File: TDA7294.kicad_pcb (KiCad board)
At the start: 2 copper layers, 81 x 58 mm, 38 parts, among them J1 PAWER, J2 OUT, J3 IN, U1 TDA7294, U2 TDA7294

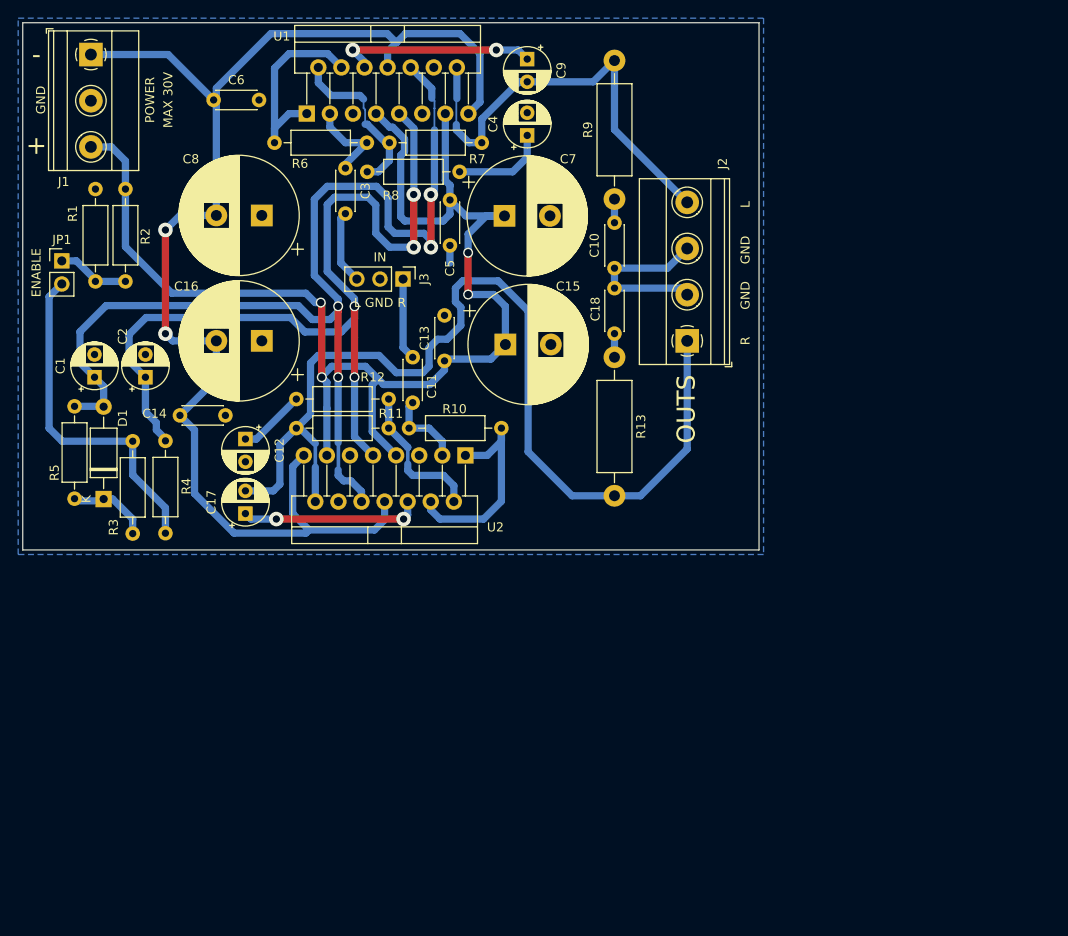
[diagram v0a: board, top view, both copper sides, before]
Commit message: agregando huecos para montaje
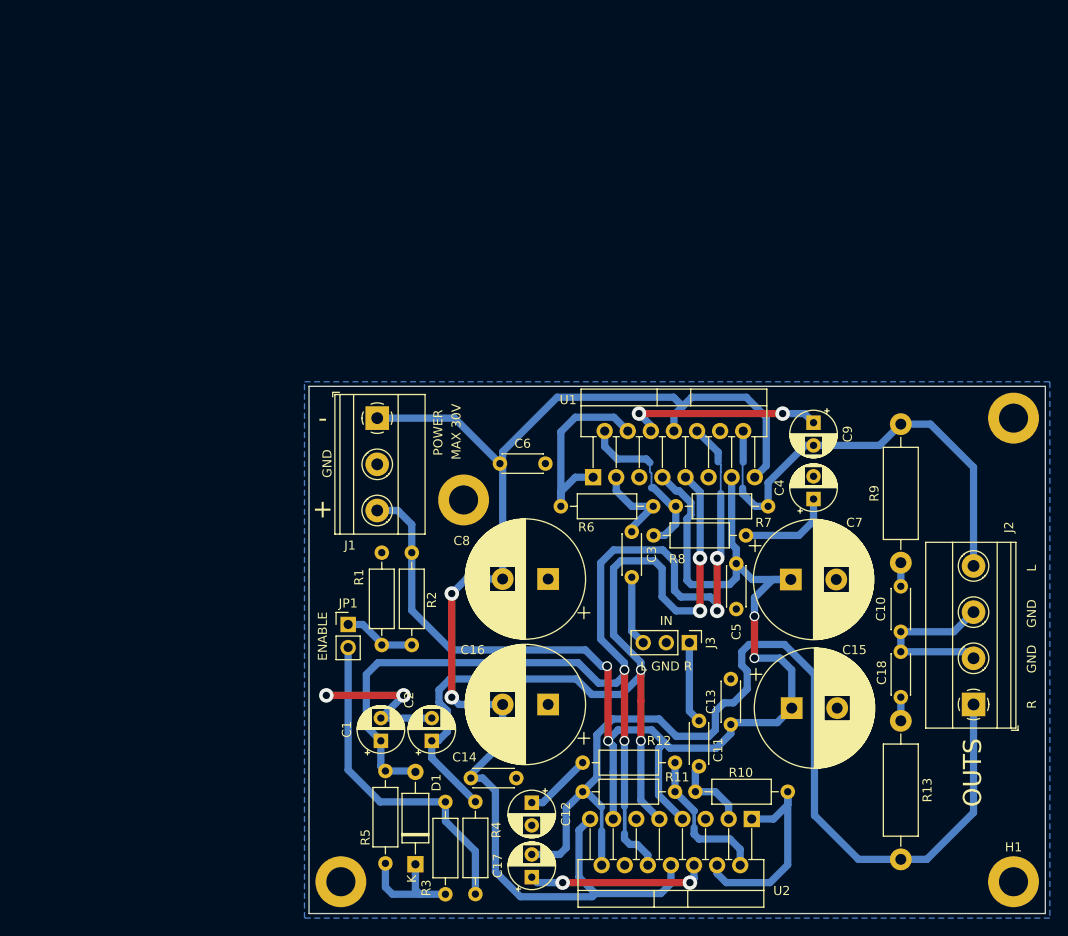
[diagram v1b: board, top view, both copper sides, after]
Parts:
- added H1: MH, MountingHole:MountingHole_3.2mm_M3_DIN965_Pad, F.Cu at (184.5, 124.5)
- added H2: MH, MountingHole:MountingHole_3.2mm_M3_DIN965_Pad, F.Cu at (110.5, 124.5)
- added H3: MH, MountingHole:MountingHole_3.2mm_M3_DIN965_Pad, F.Cu at (184.5, 73.5)
- added H4: MH, MountingHole:MountingHole_3.2mm_M3_DIN965_Pad, F.Cu at (124.0, 82.5)
- moved D1 52.8 mm to (118.7, 122.6)
- moved R5 52.7 mm to (115.4, 112.3)
- moved R3 52.5 mm to (122.0, 125.9)
- moved R4 52.3 mm to (125.3, 115.7)
- moved C14 51.1 mm to (124.8, 113.1)
- moved C16 50.9 mm to (133.3, 105.0)
- moved C4 50.9 mm to (162.5, 82.4)
- moved C8 50.9 mm to (133.3, 91.2)
- moved R7 50.9 mm to (144.9, 86.4)
- moved R9 50.9 mm to (172.1, 89.4)
- moved C1 50.9 mm to (114.9, 109.0)
- moved C10 50.9 mm to (172.1, 97.0)
- moved C11 50.9 mm to (149.9, 111.8)
- moved C12 50.9 mm to (131.5, 115.8)
- moved C13 50.9 mm to (153.4, 107.2)
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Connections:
- U1 pad 11: (no net) -> unconnected-(U1-Pad11)
- U1 pad 12: (no net) -> unconnected-(U1-Pad12)
- U1 pad 5: (no net) -> unconnected-(U1-Pad5)
- U2 pad 11: (no net) -> unconnected-(U2-Pad11)
- U2 pad 12: (no net) -> unconnected-(U2-Pad12)
- U2 pad 5: (no net) -> unconnected-(U2-Pad5)
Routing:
- net GND: track 68.0 -> 83.7 mm, vias 0 -> 2
- net Net-(D1-Pad1): track 9.49 -> 13.1 mm
- net /MUTE: track 119.0 -> 121.0 mm
- net /OUT1: track 49.1 -> 51.0 mm
- net /STBY: track 100.6 -> 99.7 mm
- net Net-(JP1-Pad2): track 37.8 -> 37.1 mm
- net /OUT2: track 112.1 -> 111.6 mm
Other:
- board text added: "0"
- board text added: "0 mm"
- board text added: "0.01 mm"
- board text added: "0.02"
- board text added: "0.035 mm"
- board text added: "0.2000 mm / 0.0000 mm"
- board text added: "0.3000 mm"
- board text added: "1"
- board text added: "1.51 mm"
- board text added: "1.6000 mm"
- board text added: "2"
- board text added: "3.3"
- board text added: "4.5"
- board text added: "81.0000 mm x 58.0000 mm"
- board text added: "B.Cu"
- board text added: "B.Mask"
- board text added: "B.Paste"
- board text added: "B.Silkscreen"
- board text added: "BOARD CHARACTERISTICS"
- board text added: "Black"
- board text added: "Board Thickness:"
- board text added: "Board overall dimensions:"
- board text added: "Bottom Silk Screen"
- board text added: "Bottom Solder Mask"
- board text added: "Bottom Solder Paste"
- board text added: "Castellated pads:"
- board text added: "Color"
- board text added: "Copper Finish:"
- board text added: "Copper Layer Count:"
- board text added: "Dielectric 1"
- board text added: "Direct Printing"
- board text added: "Edge card connectors:"
- board text added: "Epsilon R"
- board text added: "F.Cu"
- board text added: "F.Mask"
- board text added: "F.Paste"
- board text added: "F.Silkscreen"
- board text added: "FR4"
- board text added: "HAL SnPb"
- board text added: "Impedance Control:"
- board text added: "Layer Name"
- board text added: "Liquid Ink"
- board text added: "Loss Tangent"
- board text added: "Material"
- board text added: "Min hole diameter:"
- board text added: "Min track/spacing:"
- board text added: "No"
- board text added: "Plated Board Edge:"
- board text added: "Thickness (mm)"
- board text added: "Top Silk Screen"
- board text added: "Top Solder Mask"
- board text added: "Top Solder Paste"
- board text added: "Type"
- board text added: "White"
- board text added: "copper"
- board text added: "core"

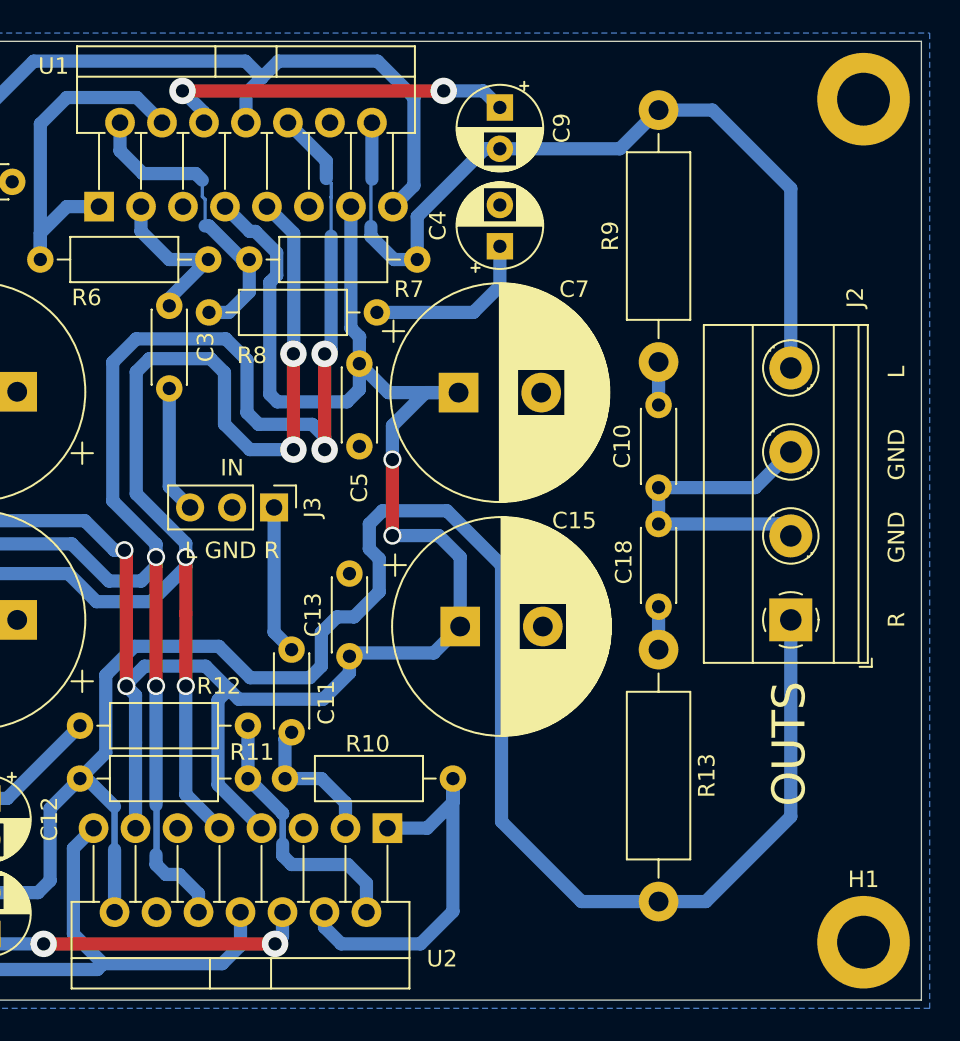
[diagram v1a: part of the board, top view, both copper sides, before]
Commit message: add version puenteable y archivos en pdf
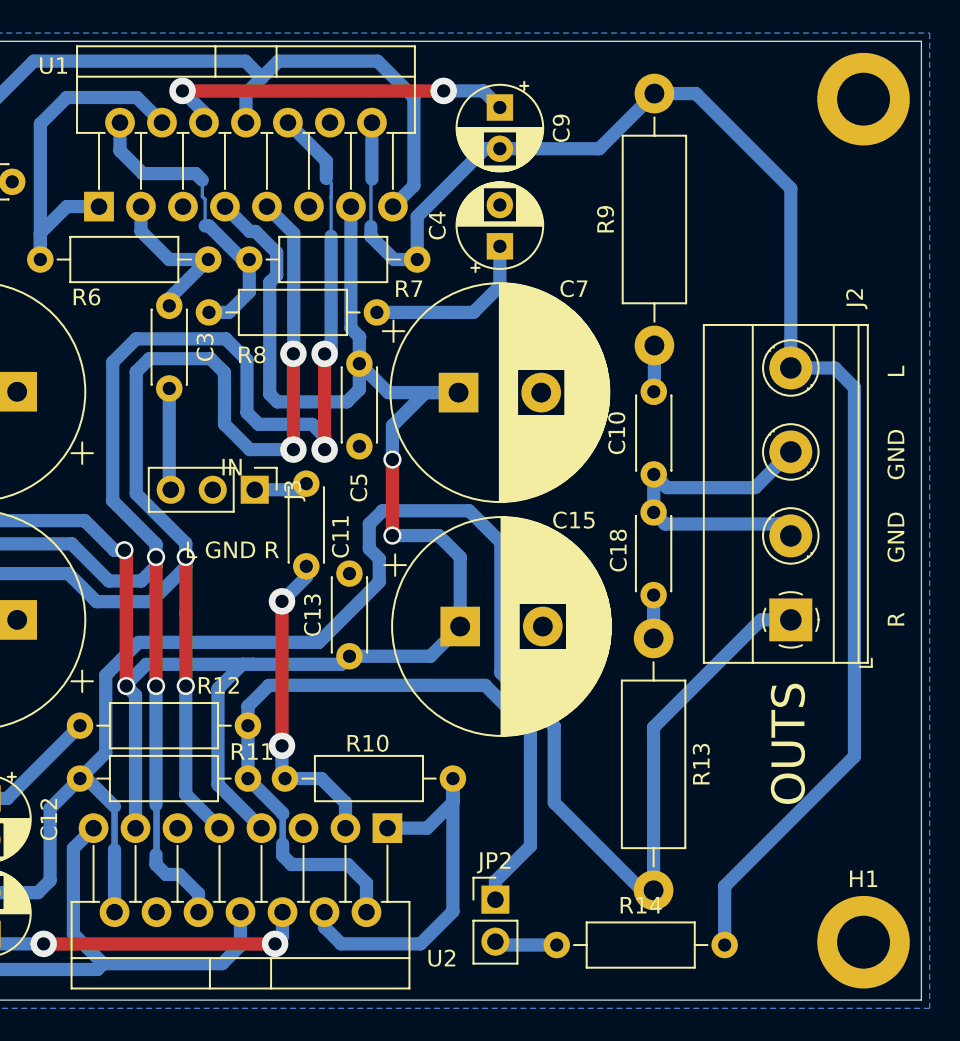
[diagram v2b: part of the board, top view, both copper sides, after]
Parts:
- added JP2: BRI, Connector_PinHeader_2.54mm:PinHeader_1x02_P2.54mm_Vertical, F.Cu at (162.2, 121.9)
- added R14: 22K, Resistor_THT:R_Axial_DIN0207_L6.3mm_D2.5mm_P10.16mm_Horizontal, F.Cu at (165.9, 124.7)
- moved C11 10.1 mm to (150.8, 101.8)
- moved J3 1.59 mm to (147.7, 97.1)
- moved R9 1.03 mm to (171.8, 88.4)
- moved C10 0.85 mm to (171.8, 96.2)
- moved C18 0.76 mm to (171.8, 98.5)
- moved R13 0.74 mm to (171.8, 106.1)
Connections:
- net Net-(R11-Pad1) renamed /sheet60964E77/brig
- net Net-(R7-Pad1) renamed /Sheet6095E24E/brig
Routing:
- net /OUT1: track 51.0 -> 93.1 mm
- net /sheet60964E77/brig: track 16.1 -> 47.2 mm
- net Net-(U2-+): track 8.77 -> 19.3 mm, vias 0 -> 2
- net /OUT2: track 111.6 -> 105.0 mm
- net /IN2: track 9.04 -> 3.27 mm
- net Net-(JP2-Pad2): track 0.00 -> 3.79 mm
- net /IN1: track 7.72 -> 6.17 mm
- net GND: track 83.7 -> 85.0 mm
